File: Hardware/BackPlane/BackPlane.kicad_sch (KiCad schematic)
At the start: 5 parts

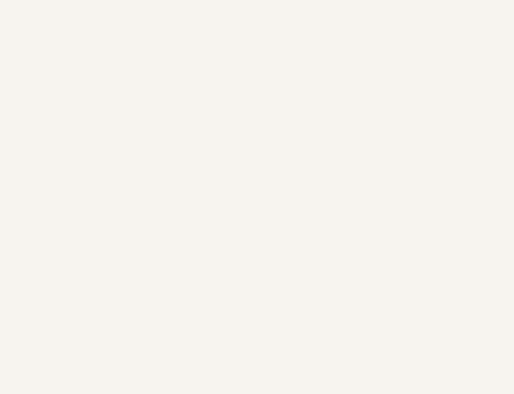
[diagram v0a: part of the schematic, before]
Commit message: Add body for backplane
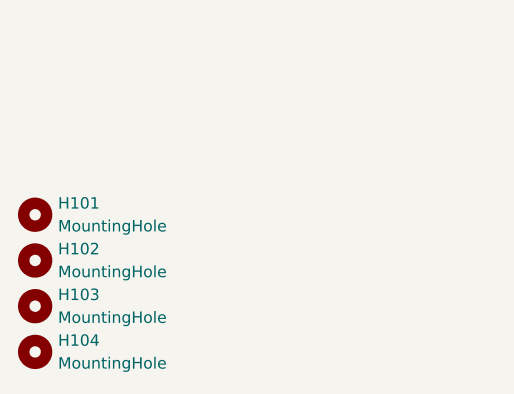
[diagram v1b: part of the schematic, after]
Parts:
- added H101, H102, H103, H104: MountingHole, MountingHole:MountingHole_3.5mm, symbol Mechanical:MountingHole
- C101: footprint (none) -> KenwoodFox:EBM15DSEH

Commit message: Bump backplane
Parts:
- added J103: Power Harness, Connector_JST:JST_EH_B5B-EH-A_1x05_P2.50mm_Vertical, symbol Connector:Conn_01x05_Socket
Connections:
- net +12V: now also C101.1, C102.1, C103.1, C104.1, C105.1, J103.5 (Pin_5); no longer C101.16, C102.16, C103.16, C104.16, C105.16
- net +5V: now also C101.16, C102.16, C103.16, C104.16, C105.16, J103.3 (Pin_3); no longer C101.1, C102.1, C103.1, C104.1, C105.1
- net GND: now also J103.1 (Pin_1)
- net CARD_EN_2: now reaches C104.14
- net CARD_EN_2: now also C101.13
- net CARD_SEL_2: now reaches C104.29
- net CARD_SEL_2: now also C101.28
- net CARD_EN_1: now reaches C103.14
- net CARD_EN_1: now also C101.12
- net CARD_SEL_1: now reaches C103.29
- net CARD_SEL_1: now also C101.27
- net CARD_EN_0: now reaches C101.11
- net CARD_EN_0: now also C102.14
- net CARD_EN_3: now reaches C101.14
- net CARD_EN_3: now also C105.14
- net CARD_SEL_0: now reaches C101.26
- net CARD_SEL_0: now also C102.29
- net CARD_SEL_3: now reaches C101.29
- net CARD_SEL_3: now also C105.29
- no-connect marks 0 -> 25

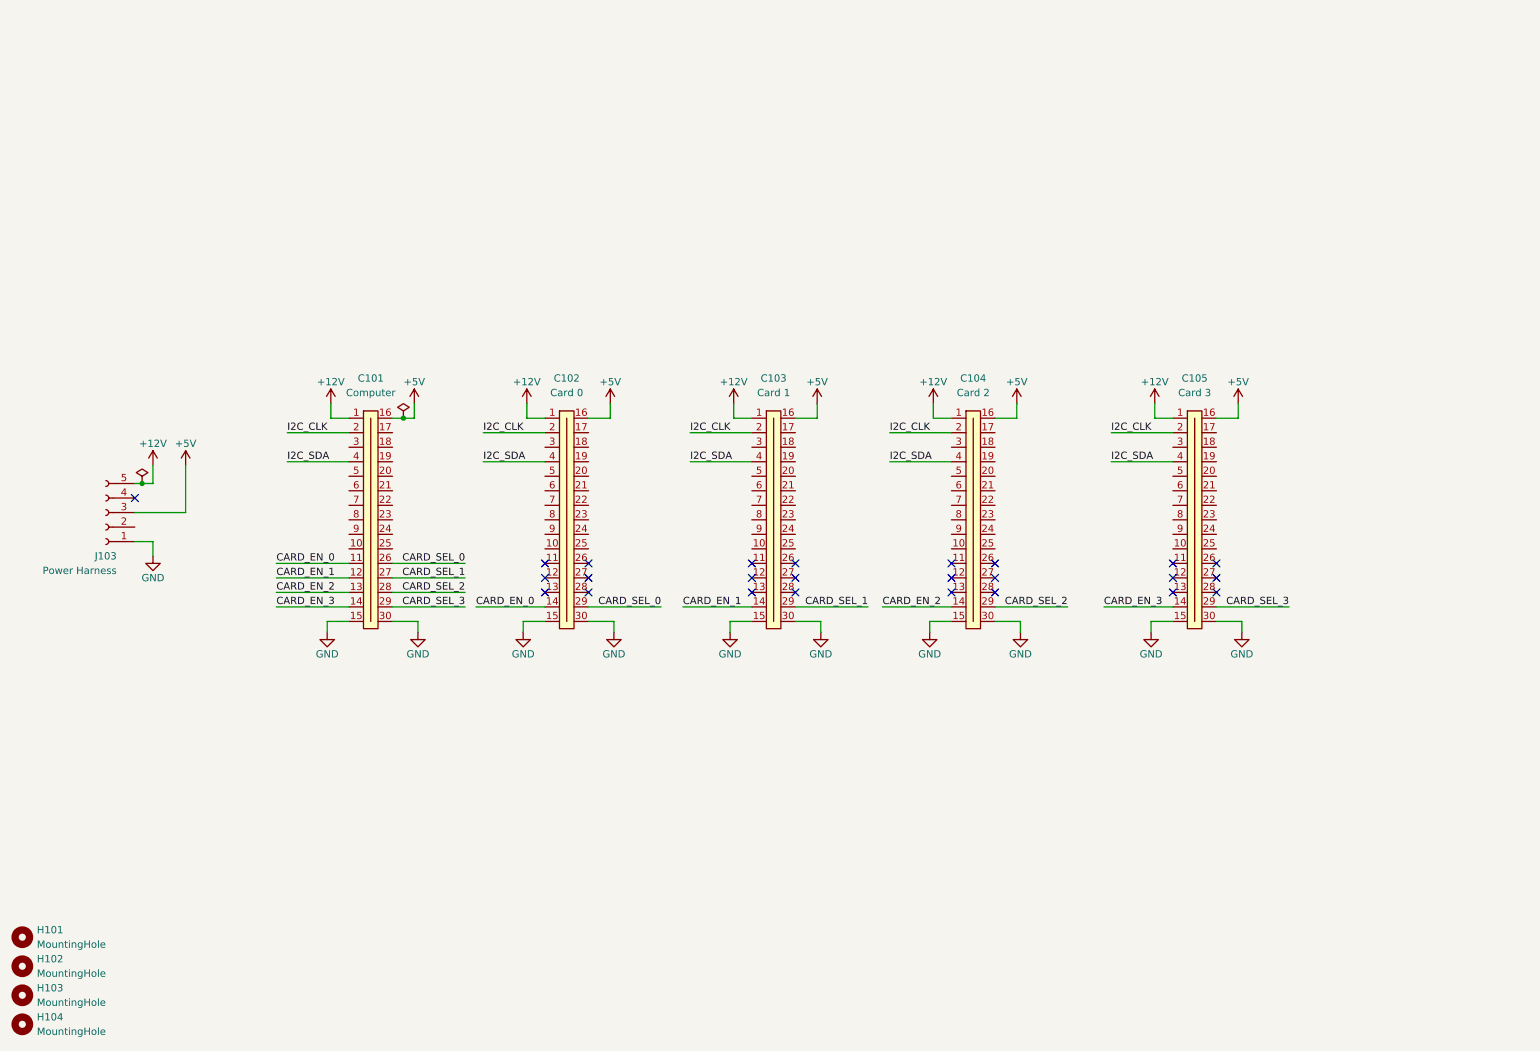
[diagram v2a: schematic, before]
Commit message: Bump everything with new backplane design
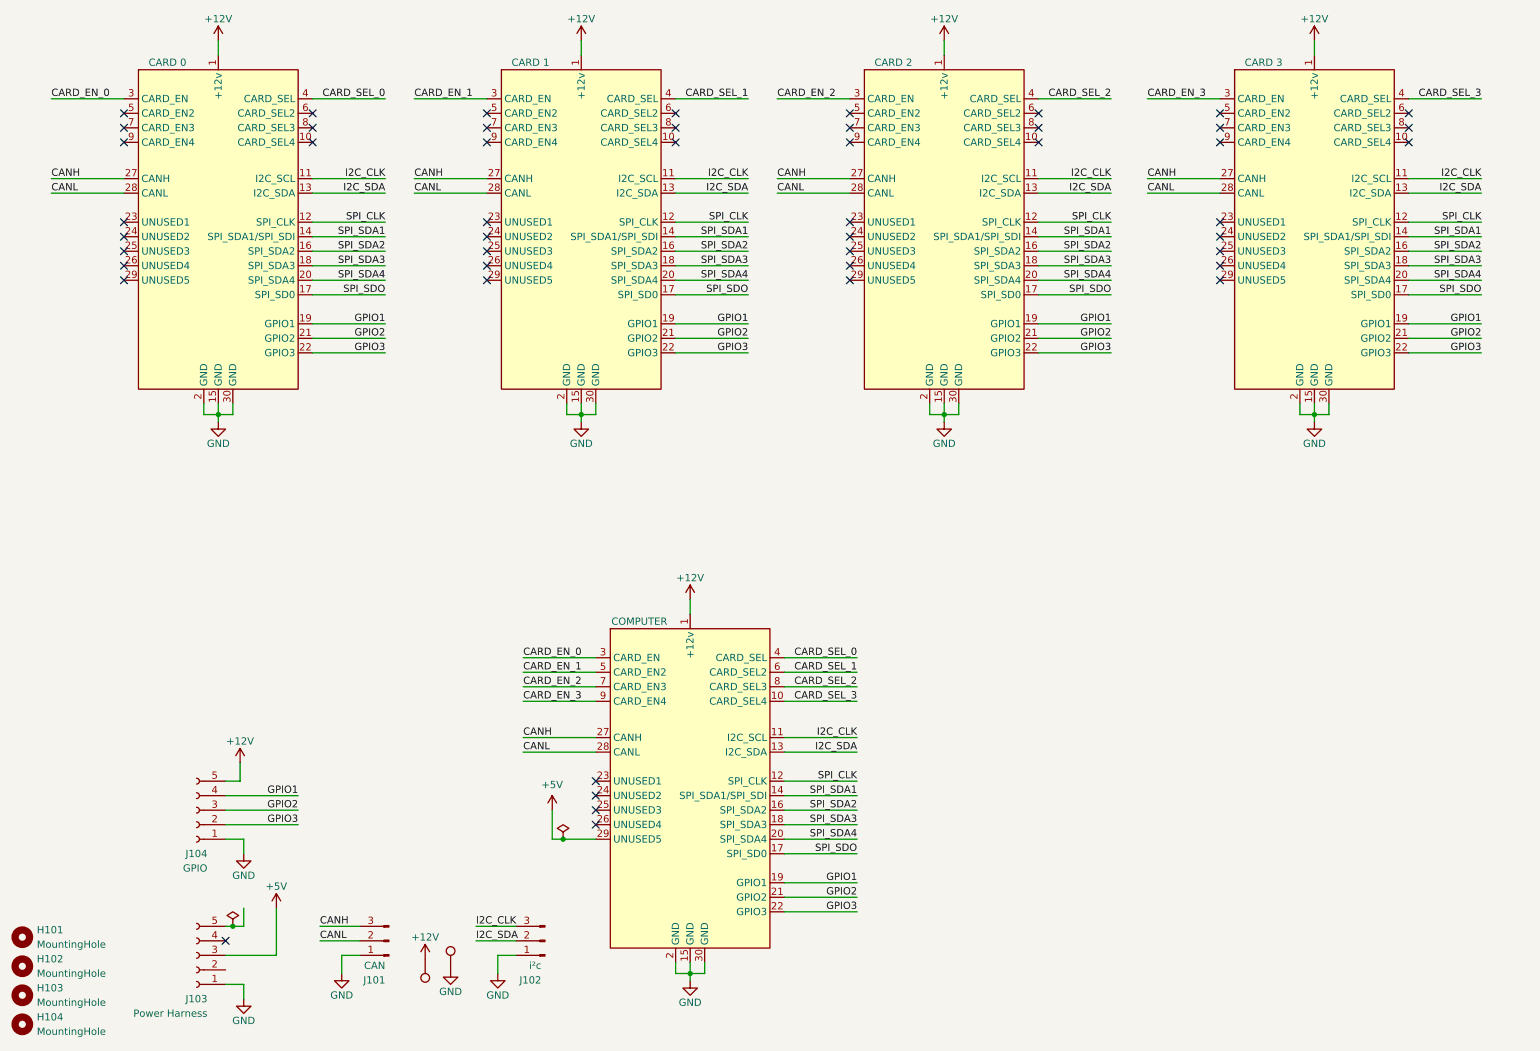
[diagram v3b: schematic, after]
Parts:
- removed C101: Computer, KenwoodFox:EBM15DSEH, symbol KenwoodFox:EBM15DSEH
- removed C102: Card 0, KenwoodFox:EBM15DSEH, symbol KenwoodFox:EBM15DSEH
- removed C103: Card 1, KenwoodFox:EBM15DSEH, symbol KenwoodFox:EBM15DSEH
- removed C104: Card 2, KenwoodFox:EBM15DSEH, symbol KenwoodFox:EBM15DSEH
- removed C105: Card 3, KenwoodFox:EBM15DSEH, symbol KenwoodFox:EBM15DSEH
- added J101: CAN, Connector_JST:JST_EH_B3B-EH-A_1x03_P2.50mm_Vertical, symbol Connector:Conn_01x03_Pin
- added J102: i²c, Connector_JST:JST_EH_B3B-EH-A_1x03_P2.50mm_Vertical, symbol Connector:Conn_01x03_Pin
- added J104: GPIO, Connector_JST:JST_EH_B5B-EH-A_1x05_P2.50mm_Vertical, symbol Connector:Conn_01x05_Socket
- added TP101, TP102: TestPoint, TestPoint:TestPoint_Loop_D2.54mm_Drill1.5mm_Beaded, symbol Connector:TestPoint
- added U101: COMPUTER, KenwoodFox:EBM15DSEH, symbol KenwoodFox:KIT_CONNECTOR
- added U102: CARD 0, KenwoodFox:EBM15DSEH, symbol KenwoodFox:KIT_CONNECTOR
- added U103: CARD 1, KenwoodFox:EBM15DSEH, symbol KenwoodFox:KIT_CONNECTOR
- added U104: CARD 2, KenwoodFox:EBM15DSEH, symbol KenwoodFox:KIT_CONNECTOR
- added U105: CARD 3, KenwoodFox:EBM15DSEH, symbol KenwoodFox:KIT_CONNECTOR
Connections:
- net +12V: now also J104.5 (Pin_5), TP101.1, U101.1 (+12v), U102.1 (+12v), U103.1 (+12v), U104.1 (+12v), U105.1 (+12v); no longer J103.5 (Pin_5)
- net +5V: now also U101.29 (UNUSED5)
- net CARD_EN_0: now also U101.3 (CARD_EN), U102.3 (CARD_EN)
- net CARD_EN_1: now also U101.5 (CARD_EN2), U103.3 (CARD_EN)
- net CARD_EN_2: now also U101.7 (CARD_EN3), U104.3 (CARD_EN)
- net CARD_EN_3: now also U101.9 (CARD_EN4), U105.3 (CARD_EN)
- net CARD_SEL_0: now also U101.4 (CARD_SEL), U102.4 (CARD_SEL)
- net CARD_SEL_1: now also U101.6 (CARD_SEL2), U103.4 (CARD_SEL)
- net CARD_SEL_2: now also U101.8 (CARD_SEL3), U104.4 (CARD_SEL)
- net CARD_SEL_3: now also U101.10 (CARD_SEL4), U105.4 (CARD_SEL)
- net GND: now also J101.1 (Pin_1), J102.1 (Pin_1), J104.1 (Pin_1), TP102.1, U101.15 (GND), U101.2 (GND), U101.30 (GND), U102.15 (GND), U102.2 (GND), U102.30 (GND), U103.15 (GND), U103.2 (GND), U103.30 (GND), U104.15 (GND), U104.2 (GND), U104.30 (GND), U105.15 (GND), U105.2 (GND), U105.30 (GND)
- net I2C_CLK: now also J102.3 (Pin_3), U101.11 (I2C_SCL), U102.11 (I2C_SCL), U103.11 (I2C_SCL), U104.11 (I2C_SCL), U105.11 (I2C_SCL)
- net I2C_SDA: now also J102.2 (Pin_2), U101.13 (I2C_SDA), U102.13 (I2C_SDA), U103.13 (I2C_SDA), U104.13 (I2C_SDA), U105.13 (I2C_SDA)
- new net CANH: J101.3 (Pin_3), U101.27 (CANH), U102.27 (CANH), U103.27 (CANH), U104.27 (CANH), U105.27 (CANH)
- new net CANL: J101.2 (Pin_2), U101.28 (CANL), U102.28 (CANL), U103.28 (CANL), U104.28 (CANL), U105.28 (CANL)
- new net GPIO1: J104.4 (Pin_4), U101.19 (GPIO1), U102.19 (GPIO1), U103.19 (GPIO1), U104.19 (GPIO1), U105.19 (GPIO1)
- new net GPIO2: J104.3 (Pin_3), U101.21 (GPIO2), U102.21 (GPIO2), U103.21 (GPIO2), U104.21 (GPIO2), U105.21 (GPIO2)
- new net GPIO3: J104.2 (Pin_2), U101.22 (GPIO3), U102.22 (GPIO3), U103.22 (GPIO3), U104.22 (GPIO3), U105.22 (GPIO3)
- new net SPI_CLK: U101.12 (SPI_CLK), U102.12 (SPI_CLK), U103.12 (SPI_CLK), U104.12 (SPI_CLK), U105.12 (SPI_CLK)
- new net SPI_SDA1: U101.14 (SPI_SDA1/SPI_SDI), U102.14 (SPI_SDA1/SPI_SDI), U103.14 (SPI_SDA1/SPI_SDI), U104.14 (SPI_SDA1/SPI_SDI), U105.14 (SPI_SDA1/SPI_SDI)
- new net SPI_SDA2: U101.16 (SPI_SDA2), U102.16 (SPI_SDA2), U103.16 (SPI_SDA2), U104.16 (SPI_SDA2), U105.16 (SPI_SDA2)
- new net SPI_SDA3: U101.18 (SPI_SDA3), U102.18 (SPI_SDA3), U103.18 (SPI_SDA3), U104.18 (SPI_SDA3), U105.18 (SPI_SDA3)
- new net SPI_SDA4: U101.20 (SPI_SDA4), U102.20 (SPI_SDA4), U103.20 (SPI_SDA4), U104.20 (SPI_SDA4), U105.20 (SPI_SDA4)
- new net SPI_SDO: U101.17 (SPI_SD0), U102.17 (SPI_SD0), U103.17 (SPI_SD0), U104.17 (SPI_SD0), U105.17 (SPI_SD0)
- no-connect marks 25 -> 49
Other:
- moved on the sheet: J103

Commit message: Add all
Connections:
- net +12V: now also J103.5 (Pin_5)
- net +5V: now also U102.29 (UNUSED5), U103.29 (UNUSED5), U104.29 (UNUSED5), U105.29 (UNUSED5)
- net UNUSED1: now reaches U102.23 (UNUSED1)
- net UNUSED1: now also U101.23 (UNUSED1), U103.23 (UNUSED1), U104.23 (UNUSED1), U105.23 (UNUSED1)
- net UNUSED2: now reaches U102.24 (UNUSED2)
- net UNUSED2: now also U101.24 (UNUSED2), U103.24 (UNUSED2), U104.24 (UNUSED2), U105.24 (UNUSED2)
- net UNUSED3: now reaches U102.25 (UNUSED3)
- net UNUSED3: now also U101.25 (UNUSED3), U103.25 (UNUSED3), U104.25 (UNUSED3), U105.25 (UNUSED3)
- net UNUSED4: now reaches U102.26 (UNUSED4)
- net UNUSED4: now also U101.26 (UNUSED4), U103.26 (UNUSED4), U104.26 (UNUSED4), U105.26 (UNUSED4)
- no-connect marks 49 -> 25
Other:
- moved on the sheet: J104
